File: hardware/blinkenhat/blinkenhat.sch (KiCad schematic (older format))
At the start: 25 parts, among them J1 Conn_01x03, J2 Conn_01x03, J3 Conn_01x03, J4 Programmer, J5 USB_OTG, Q1 2N7002, Q2 2N7002, SW1 RESET, U1 AMS1117-3V3, U2 ESP-12E

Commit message: Hardware: update schematics names.
Signed-off-by: Jan Losinski <losinski@wh2.tu-dresden.de>
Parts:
- J1: value Conn_01x03 -> LED1
- J2: value Conn_01x03 -> LED2
- J3: value Conn_01x03 -> INPUT
- J5: value USB_OTG -> USB_POWER
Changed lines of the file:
@@
 P 4250 4100
 F 0 "J5" H 4050 4550 50  0000 L CNN
-F 1 "USB_OTG" H 4050 4450 50  0000 L CNN
+F 1 "USB_POWER" H 4050 4450 50  0000 L CNN
 F 2 "Connectors:USB_Micro-B_10103594-0001LF" H 4400 4050 50  0001 C CNN
 F 3 "" H 4400 4050 50  0001 C CNN
@@
 P 2000 4250
 F 0 "J3" H 2000 4450 50  0000 C CNN
-F 1 "Conn_01x03" H 2000 4050 50  0000 C CNN
+F 1 "INPUT" H 2000 4050 50  0000 C CNN
 F 2 "Connectors_JST:JST_XH_B03B-XH-A_03x2.50mm_Straight" H 2000 4250 50  0001 C CNN
 F 3 "" H 2000 4250 50  0001 C CNN
@@
 P 1800 6800
 F 0 "J2" H 1800 7000 50  0000 C CNN
-F 1 "Conn_01x03" H 1800 6600 50  0000 C CNN
+F 1 "LED2" H 1800 6600 50  0000 C CNN
 F 2 "Connectors_JST:JST_XH_B03B-XH-A_03x2.50mm_Straight" H 1800 6800 50  0001 C CNN
 F 3 "" H 1800 6800 50  0001 C CNN
@@
 P 1800 6250
 F 0 "J1" H 1800 6450 50  0000 C CNN
-F 1 "Conn_01x03" H 1800 6050 50  0000 C CNN
+F 1 "LED1" H 1800 6050 50  0000 C CNN
 F 2 "Connectors_JST:JST_XH_B03B-XH-A_03x2.50mm_Straight" H 1800 6250 50  0001 C CNN
 F 3 "" H 1800 6250 50  0001 C CNN

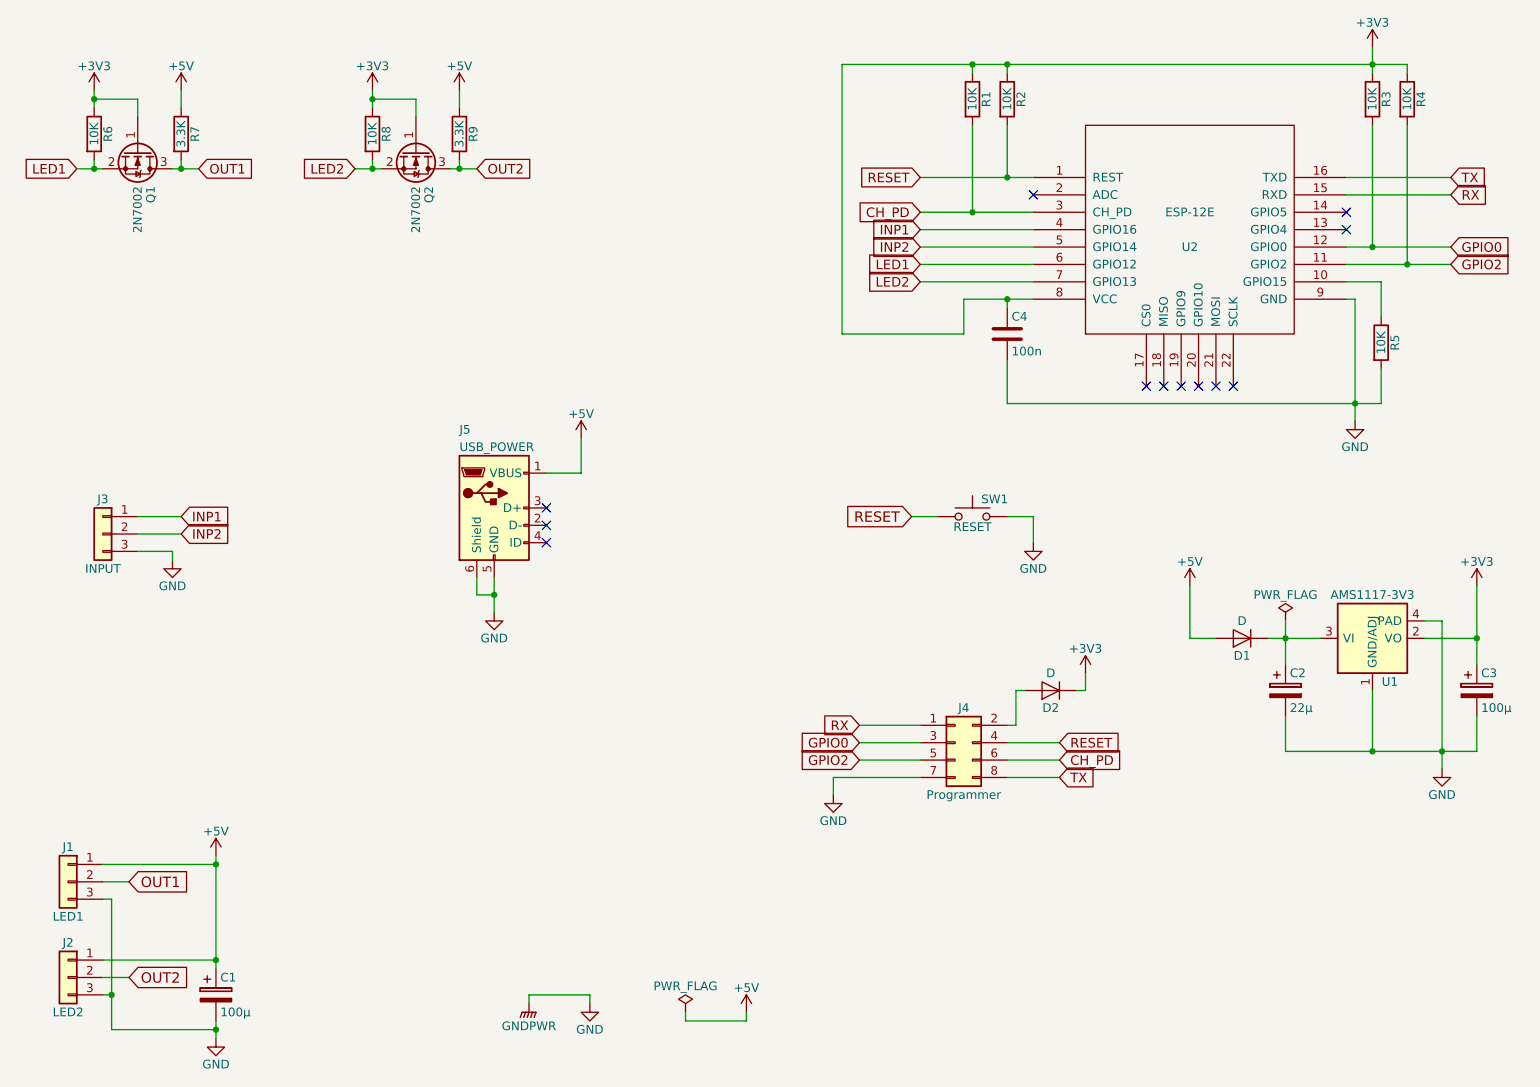
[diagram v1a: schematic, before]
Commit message: Hardware: Add GPIO Header to schematic.
Signed-off-by: Jan Losinski <losinski@wh2.tu-dresden.de>
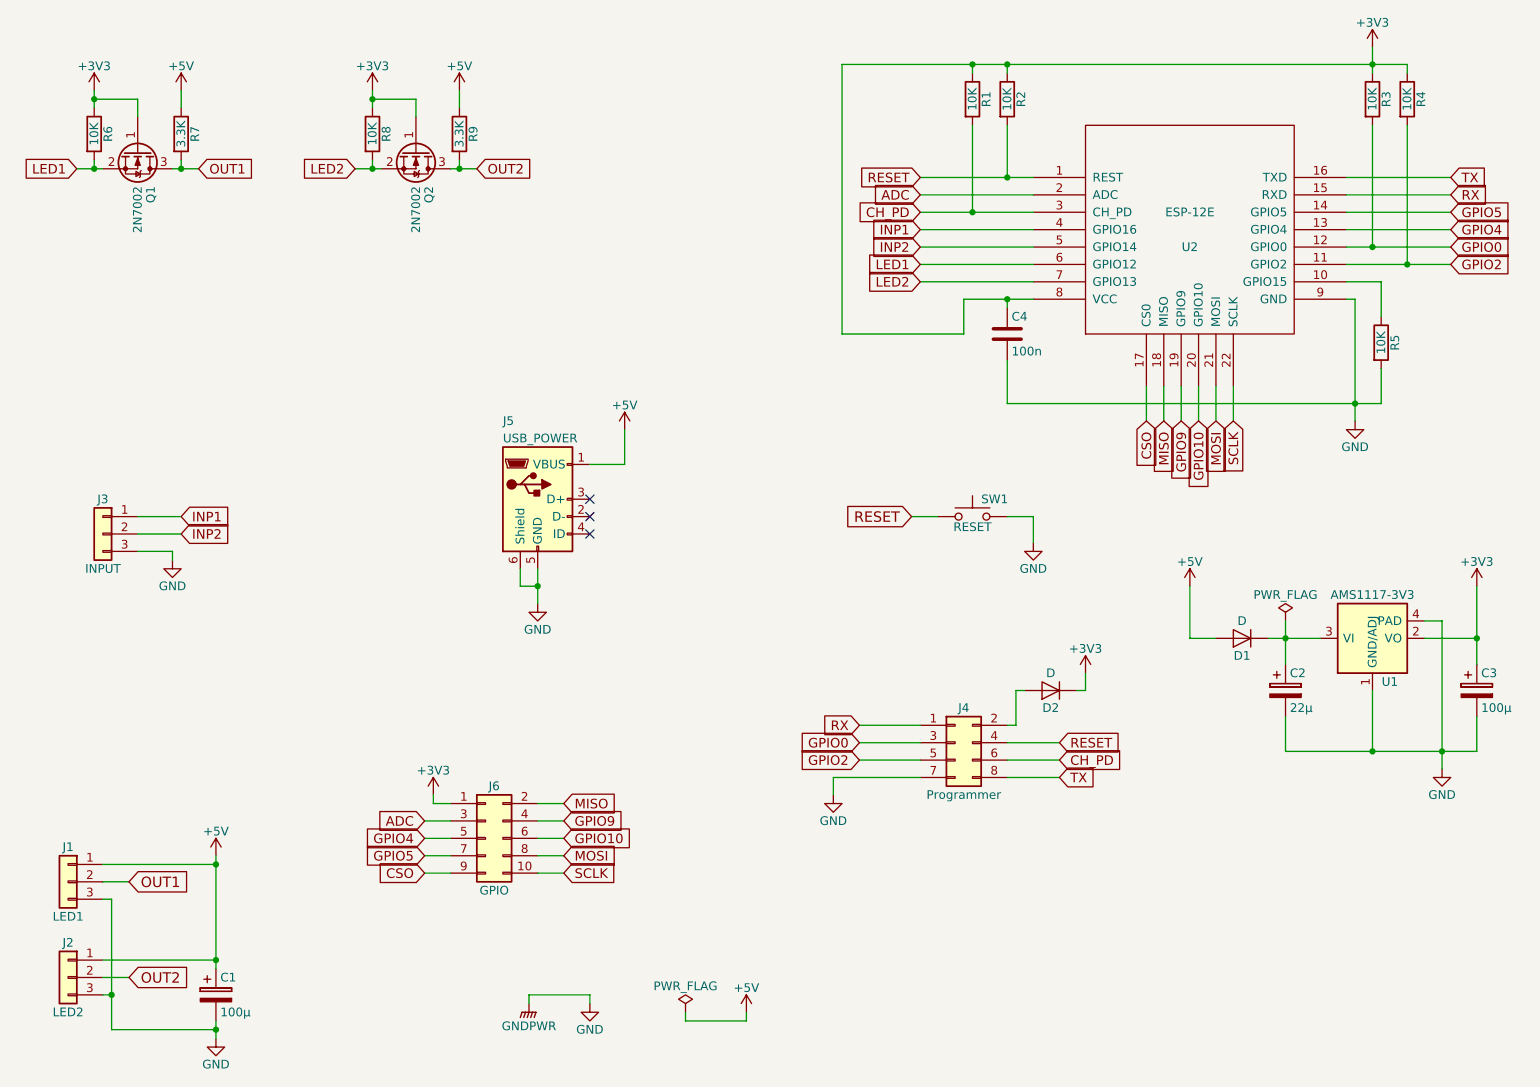
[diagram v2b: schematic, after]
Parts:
- added J6: GPIO, Pin_Headers:Pin_Header_Straight_2x05_Pitch1.27mm, symbol Conn_02x05_Odd_Even
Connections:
- net +3V3: now also J6.1 (Pin_1)
- net GPIO4: now reaches U2.13 (GPIO4)
- net GPIO4: now also J6.5 (Pin_5)
- net GPIO5: now reaches U2.14 (GPIO5)
- net GPIO5: now also J6.7 (Pin_7)
- net CSO: now reaches U2.17 (CS0)
- net CSO: now also J6.9 (Pin_9)
- net MISO: now reaches U2.18 (MISO)
- net MISO: now also J6.2 (Pin_2)
- net GPIO9: now reaches U2.19 (GPIO9)
- net GPIO9: now also J6.4 (Pin_4)
- net ADC: now reaches U2.2 (ADC)
- net ADC: now also J6.3 (Pin_3)
- net GPIO10: now reaches U2.20 (GPIO10)
- net GPIO10: now also J6.6 (Pin_6)
- net MOSI: now reaches U2.21 (MOSI)
- net MOSI: now also J6.8 (Pin_8)
- net SCLK: now reaches U2.22 (SCLK)
- net SCLK: now also J6.10 (Pin_10)
- no-connect marks 12 -> 3
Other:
- moved on the sheet: J5
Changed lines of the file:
@@
 L USB_OTG J5
 U 1 1 5A4D6874
-P 4250 4100
-F 0 "J5" H 4050 4550 50  0000 L CNN
-F 1 "USB_POWER" H 4050 4450 50  0000 L CNN
-F 2 "Connectors:USB_Micro-B_10103594-0001LF" H 4400 4050 50  0001 C CNN
-F 3 "" H 4400 4050 50  0001 C CNN
-	1    4250 4100
+P 4500 4050
+F 0 "J5" H 4300 4500 50  0000 L CNN
+F 1 "USB_POWER" H 4300 4400 50  0000 L CNN
+F 2 "Connectors:USB_Micro-B_10103594-0001LF" H 4650 4000 50  0001 C CNN
+F 3 "" H 4650 4000 50  0001 C CNN
+	1    4500 4050
 	1    0    0    -1
 $EndComp
@@
 	1    0    0    -1
 $EndComp
-NoConn ~ 4550 4100
-NoConn ~ 4550 4200
-NoConn ~ 4550 4300
+NoConn ~ 4800 4050
+NoConn ~ 4800 4150
+NoConn ~ 4800 4250
 $Comp
 L C C4
@@
 L +5V #PWR04
 U 1 1 5A4D82F4
-P 4750 3700
-F 0 "#PWR04" H 4750 3550 50  0001 C CNN
-F 1 "+5V" H 4750 3840 50  0000 C CNN
-F 2 "" H 4750 3700 50  0001 C CNN
-F 3 "" H 4750 3700 50  0001 C CNN
-	1    4750 3700
+P 5000 3650
+F 0 "#PWR04" H 5000 3500 50  0001 C CNN
+F 1 "+5V" H 5000 3790 50  0000 C CNN
+F 2 "" H 5000 3650 50  0001 C CNN
+F 3 "" H 5000 3650 50  0001 C CNN
+	1    5000 3650
 	1    0    0    -1
 $EndComp
@@
 L GND #PWR05
 U 1 1 5A4D832A
-P 4250 4700
-F 0 "#PWR05" H 4250 4450 50  0001 C CNN
-F 1 "GND" H 4250 4550 50  0000 C CNN
-F 2 "" H 4250 4700 50  0001 C CNN
-F 3 "" H 4250 4700 50  0001 C CNN
-	1    4250 4700
+P 4500 4650
+F 0 "#PWR05" H 4500 4400 50  0001 C CNN
+F 1 "GND" H 4500 4500 50  0000 C CNN
+F 2 "" H 4500 4650 50  0001 C CNN
+F 3 "" H 4500 4650 50  0001 C CNN
+	1    4500 4650
 	1    0    0    -1
 $EndComp
@@
 	1    0    0    -1
 $EndComp
-NoConn ~ 8000 3400
-NoConn ~ 8100 3400
-NoConn ~ 8400 3400
-NoConn ~ 8500 3400
 Text GLabel 6650 4150 0    60   Input ~ 0
 RESET
@@
 Connection ~ 9900 4850
 Wire Wire Line
-	4250 4500 4250 4700
-Wire Wire Line
-	4250 4600 4150 4600
-Wire Wire Line
-	4150 4600 4150 4500
-Connection ~ 4250 4600
-Wire Wire Line
-	4550 3900 4750 3900
-Wire Wire Line
-	4750 3900 4750 3700
+	4500 4450 4500 4650
+Wire Wire Line
+	4500 4550 4400 4550
+Wire Wire Line
+	4400 4550 4400 4450
+Connection ~ 4500 4550
+Wire Wire Line
+	4800 3850 5000 3850
+Wire Wire Line
+	5000 3850 5000 3650
 Wire Wire Line
 	6200 5650 6700 5650
@@
 	9200 2900 9200 3600
 Wire Wire Line
-	9350 3300 9350 3500
+	9350 3500 9350 3300
 Connection ~ 9500 2700
 Connection ~ 9300 2600
@@
 	6700 2800 7350 2800
 Wire Wire Line
-	7350 2900 6950 2900
+	6950 2900 7350 2900
 Wire Wire Line
 	6950 2900 6950 3100
@@
 	9500 1550 9500 1600
 Connection ~ 9300 1550
-NoConn ~ 8200 3400
-NoConn ~ 8300 3400
-NoConn ~ 9150 2400
-NoConn ~ 9150 2500
-NoConn ~ 7350 2300
-Wire Wire Line
-	9350 3500 7200 3500
+Wire Wire Line
+	7200 3500 9350 3500
 Wire Wire Line
 	7200 3500 7200 3250
@@
 	2000 6150 2650 6150
 Wire Wire Line
-	2000 6700 2650 6700
+	2650 6700 2000 6700
 Wire Wire Line
 	2000 6350 2050 6350
@@
 	1    0    0    -1
 $EndComp
+$Comp
+L Conn_02x05_Odd_Even J6
+U 1 1 5A4EBCE1
+P 4200 6000
+F 0 "J6" H 4250 6300 50  0000 C CNN
+F 1 "GPIO" H 4250 5700 50  0000 C CNN
+F 2 "Pin_Headers:Pin_Header_Straight_2x05_Pitch1.27mm" H 4200 6000 50  0001 C CNN
+F 3 "" H 4200 6000 50  0001 C CNN
+	1    4200 6000
+	1    0    0    -1
+$EndComp
+Text GLabel 6700 2300 0    55   Input ~ 0
+ADC
+Text GLabel 9750 2400 2    55   Input ~ 0
+GPIO5
+Text GLabel 9750 2500 2    55   Input ~ 0
+GPIO4
+Text GLabel 8200 3600 3    55   Input ~ 0
+GPIO9
+Text GLabel 8300 3600 3    55   Input ~ 0
+GPIO10
+Text GLabel 8400 3600 3    55   Input ~ 0
+MOSI
+Text GLabel 8500 3600 3    55   Input ~ 0
+SCLK
+Text GLabel 8100 3600 3    55   Input ~ 0
+MISO
+Text GLabel 8000 3600 3    55   Input ~ 0
+CSO
+Wire Wire Line
+	9750 2400 9150 2400
+Wire Wire Line
+	9150 2500 9750 2500
+Wire Wire Line
+	7350 2300 6700 2300
+Wire Wire Line
+	8000 3400 8000 3600
+Wire Wire Line
+	8100 3400 8100 3600
+Wire Wire Line
+	8200 3400 8200 3600
+Wire Wire Line
+	8300 3400 8300 3600
+Wire Wire Line
+	8400 3400 8400 3600
+Wire Wire Line
+	8500 3400 8500 3600
+Text GLabel 3850 5900 0    55   Input ~ 0
+ADC
+Text GLabel 3850 6100 0    55   Input ~ 0
+GPIO5
+Text GLabel 3850 6000 0    55   Input ~ 0
+GPIO4
+Text GLabel 3850 6200 0    55   Input ~ 0
+CSO
+Text GLabel 4650 5800 2    55   Input ~ 0
+MISO
+Text GLabel 4650 5900 2    55   Input ~ 0
+GPIO9
+Text GLabel 4650 6000 2    55   Input ~ 0
+GPIO10
+Text GLabel 4650 6100 2    55   Input ~ 0
+MOSI
+Text GLabel 4650 6200 2    55   Input ~ 0
+SCLK
+Wire Wire Line
+	3850 5900 4000 5900
+Wire Wire Line
+	4000 6000 3850 6000
+Wire Wire Line
+	3850 6100 4000 6100
+Wire Wire Line
+	4000 6200 3850 6200
+Wire Wire Line
+	4650 6200 4500 6200
+Wire Wire Line
+	4650 6100 4500 6100
+Wire Wire Line
+	4650 6000 4500 6000
+Wire Wire Line
+	4650 5900 4500 5900
+Wire Wire Line
+	4650 5800 4500 5800
+$Comp
+L +3V3 #PWR023
+U 1 1 5A4ED188
+P 3900 5750
+F 0 "#PWR023" H 3900 5600 50  0001 C CNN
+F 1 "+3V3" H 3900 5890 50  0000 C CNN
+F 2 "" H 3900 5750 50  0001 C CNN
+F 3 "" H 3900 5750 50  0001 C CNN
+	1    3900 5750
+	1    0    0    -1
+$EndComp
+Wire Wire Line
+	3900 5750 3900 5800
+Wire Wire Line
+	3900 5800 4000 5800
 $EndSCHEMATC

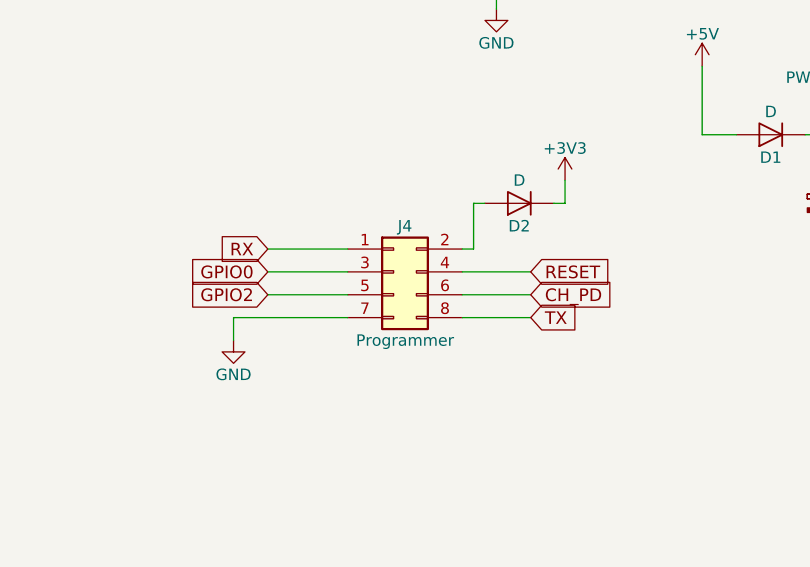
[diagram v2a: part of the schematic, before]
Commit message: Hardware: flip programmer connector.
Signed-off-by: Jan Losinski <losinski@wh2.tu-dresden.de>
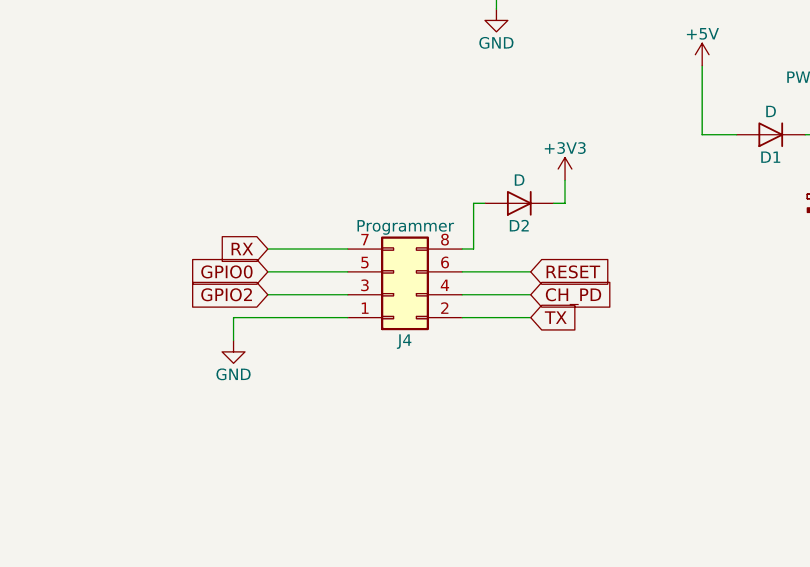
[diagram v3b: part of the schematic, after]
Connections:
- net CH_PD: now also J4.4 (Pin_4); no longer J4.6 (Pin_6)
- net GND: now also J4.1 (Pin_1); no longer J4.7 (Pin_7)
- net GPIO0: now also J4.5 (Pin_5); no longer J4.3 (Pin_3)
- net GPIO2: now also J4.3 (Pin_3); no longer J4.5 (Pin_5)
- net RESET: now also J4.6 (Pin_6); no longer J4.4 (Pin_4)
- net RX: now also J4.7 (Pin_7); no longer J4.1 (Pin_1)
- net TX: now also J4.2 (Pin_2); no longer J4.8 (Pin_8)
- net at D2.2 (A): now also J4.8 (Pin_8); no longer J4.2 (Pin_2)
